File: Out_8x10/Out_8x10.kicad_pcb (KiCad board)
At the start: 2 copper layers, 100 x 100 mm, 162 parts, among them J1 Conn_01x06, J2 nmount SW Debug, J3 USB_C_Receptacle_USB2.0, J4 Conn_01x06, J5 Conn_01x09, J6 Conn_01x10, J7 Conn_01x09, J8 Conn_01x12, Q1 2N7002, Q10 AO3401A, Q11 AO3401A, Q12 AO3401A, Q13 2N7002, Q14 2N7002, Q15 AO3401A, Q16 AO3401A, Q17 AO3400A, Q18 AO3400A, Q19 AO3400A, Q2 2N7002, Q20 AO3400A, Q21 AO3400A, Q22 AO3400A, Q23 AO3400A, Q24 AO3400A, Q25 AO3400A, Q26 AO3400A, Q3 2N7002, Q4 AO3401A, Q5 AO3401A, Q6 AO3401A, Q7 2N7002, Q8 2N7002, Q9 2N7002, SW1 Reset, SW2 Boot, SW3 ADDRESS, U1 ADM3483, U10 L78L24_SOT89, U11 L78L24_SOT89, U12 L78L24_SOT89, U13 L78L24_SOT89, U2 W25Q128JVSIQ, U3 RP2040, U4 SN74AHCT1G125, U5 AP2112K-3.3, U6 L78L24_SOT89, U7 L78L24_SOT89, U8 L78L24_SOT89, U9 L78L24_SOT89, Y1 12MHz,18pF

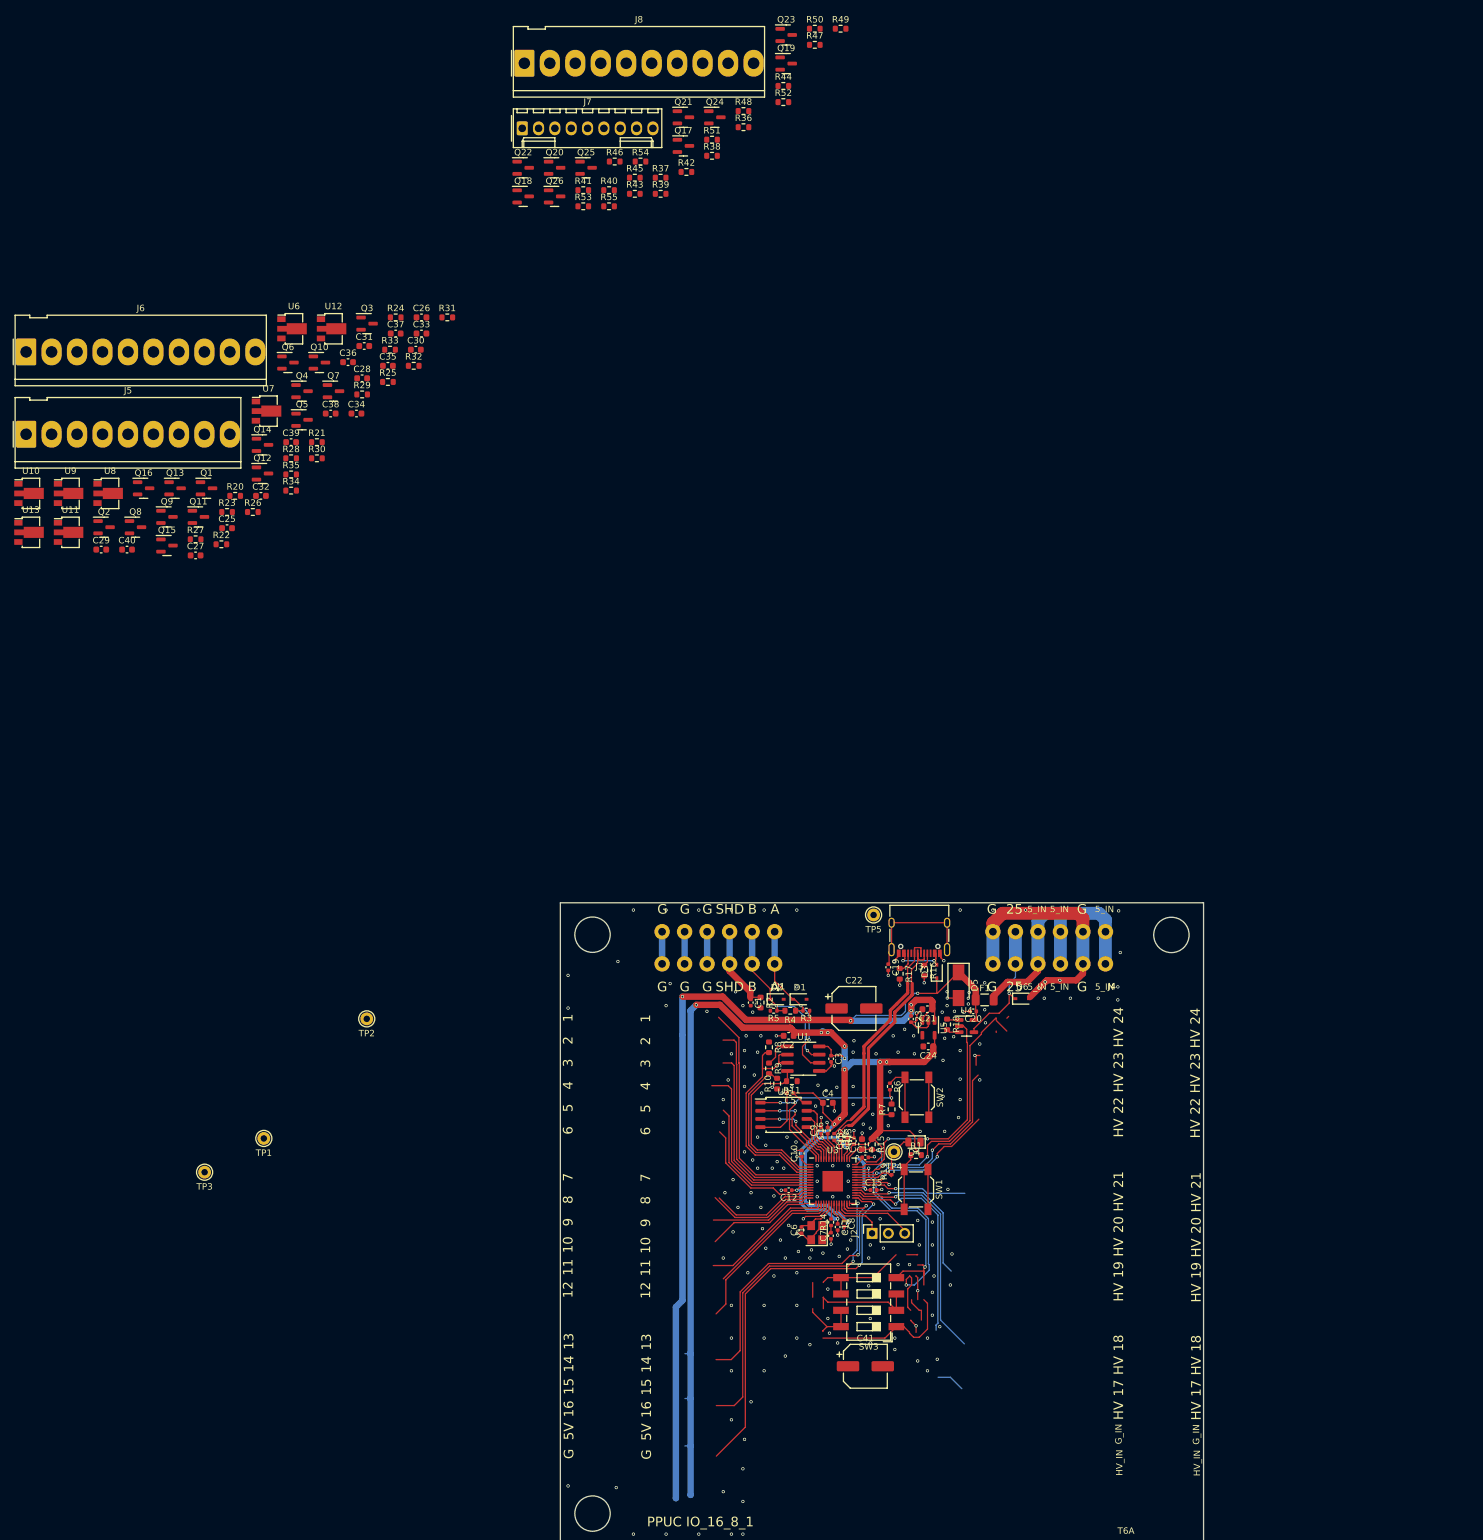
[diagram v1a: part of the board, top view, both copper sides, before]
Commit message: updated layout
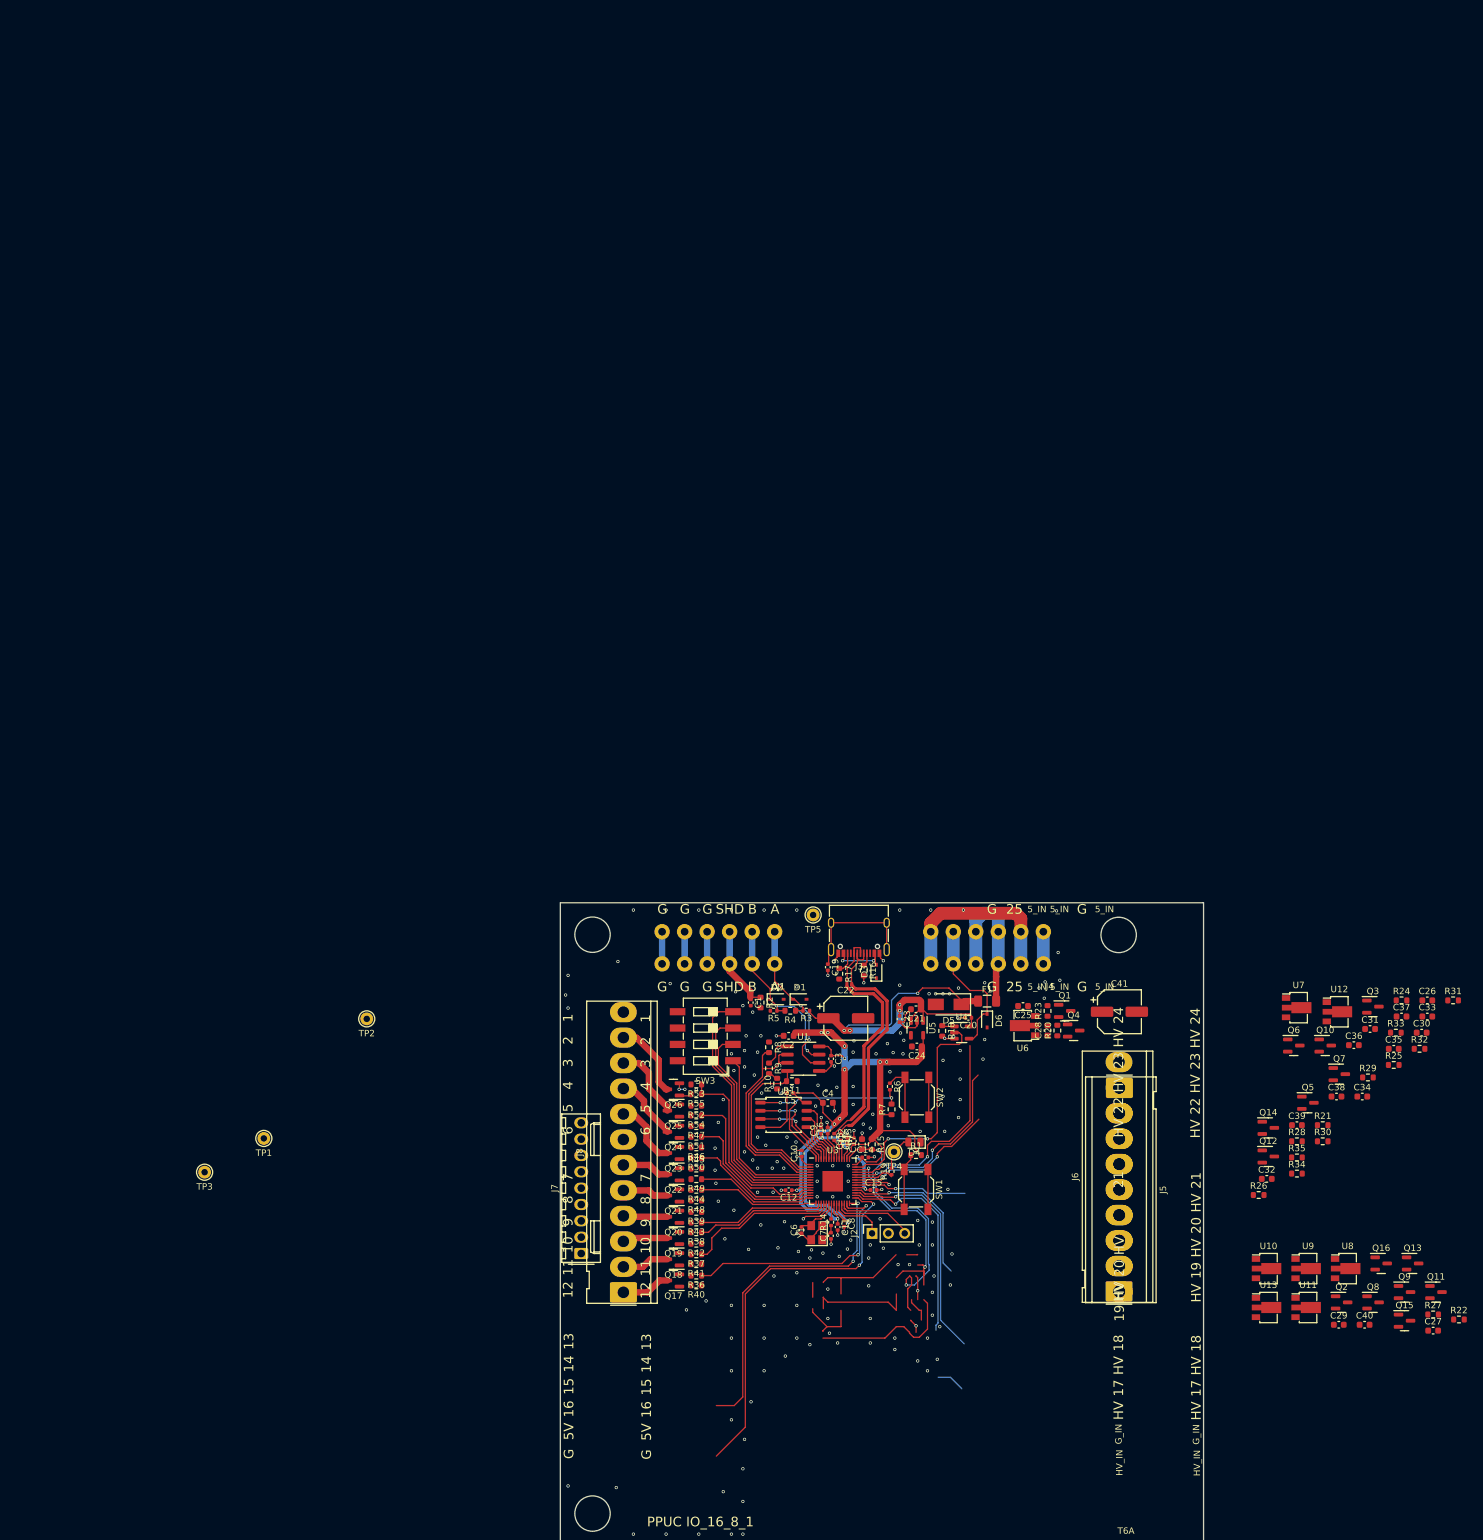
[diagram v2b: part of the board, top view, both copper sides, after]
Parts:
- J8: footprint Connector_Molex:Molex_KK-396_5273-10A_1x10_P3.96mm_Vertical -> Connector_Molex:Molex_KK-396_5273-12A_1x12_P3.96mm_Vertical
- moved C27 227.0 mm to (238.9, 111.3)
- moved R27 227.0 mm to (238.9, 108.8)
- moved U11 227.0 mm to (219.1, 107.7)
- moved U9 227.0 mm to (219.1, 101.7)
- moved C29 227.0 mm to (224.2, 110.4)
- moved C40 227.0 mm to (228.2, 110.4)
- moved Q11 227.0 mm to (239.3, 105.3)
- moved Q13 227.0 mm to (235.7, 100.9)
- moved Q15 227.0 mm to (234.4, 109.8)
- moved Q16 227.0 mm to (230.8, 100.9)
- moved Q2 227.0 mm to (224.7, 106.9)
- moved Q8 227.0 mm to (229.6, 106.9)
- moved Q9 227.0 mm to (234.4, 105.3)
- moved R22 227.0 mm to (242.9, 109.6)
- moved U10 227.0 mm to (213.0, 101.7)
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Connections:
- U3 pad 11: /Hi_6 -> /Lo_9
- U3 pad 12: /Hi_7 -> /Lo_8
- U3 pad 13: /Hi_8 -> /Lo_7
- U3 pad 14: /Lo_1 -> /Lo_6
- U3 pad 15: /Lo_2 -> /Lo_5
- U3 pad 16: /Lo_3 -> /Lo_4
- U3 pad 17: /Lo_4 -> /Lo_3
- U3 pad 18: /Lo_5 -> /Lo_2
- U3 pad 27: /Lo_6 -> /Lo_1
- U3 pad 28: /Lo_7 -> /Hi_1
- U3 pad 29: /Lo_8 -> /Hi_2
- U3 pad 30: /Lo_9 -> /Hi_3
- U3 pad 31: /Lo_10 -> /Hi_4
- U3 pad 32: /DIP_1 -> /Hi_5
- U3 pad 34: /DIP_2 -> /Hi_6
- U3 pad 35: /DIP_3 -> /Hi_7
- U3 pad 36: /DIP_4 -> /Hi_8
- U3 pad 5: /Hi_1 -> /DIP_1
- U3 pad 6: /Hi_2 -> /DIP_2
- U3 pad 7: /Hi_3 -> /DIP_3
- U3 pad 8: /Hi_4 -> /DIP_4
- U3 pad 9: /Hi_5 -> /Lo_10
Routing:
- net +3V3: track 244.5 -> 146.3 mm, vias 15 -> 14
- net +5V: track 161.7 -> 66.9 mm, vias 5 -> 7
- net /Lo_8: track 60.4 -> 23.2 mm, vias 2 -> 0
- net /DIP_2: track 17.7 -> 50.2 mm, vias 1 -> 0
- net GND: track 161.2 -> 130.6 mm, vias 206 -> 196
- net /Lo_7: track 50.7 -> 20.2 mm, vias 2 -> 0
- net /Lo_6: track 46.1 -> 18.7 mm, vias 2 -> 0
- net /Hi_2: track 33.1 -> 60.4 mm, vias 0 -> 2
- net /Lo_1: track 16.5 -> 37.6 mm, vias 0 -> 2
- net /20V: track 0.00 -> 20.7 mm
- net /5V_IN: track 43.1 -> 23.8 mm
- net /DIP_4: track 23.7 -> 40.8 mm, vias 2 -> 0
- net /Hi_1: track 35.4 -> 50.7 mm, vias 0 -> 2
- net /DIP_3: track 22.0 -> 37.2 mm, vias 1 -> 0
- net /Lo10/L10: track 0.00 -> 12.2 mm
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
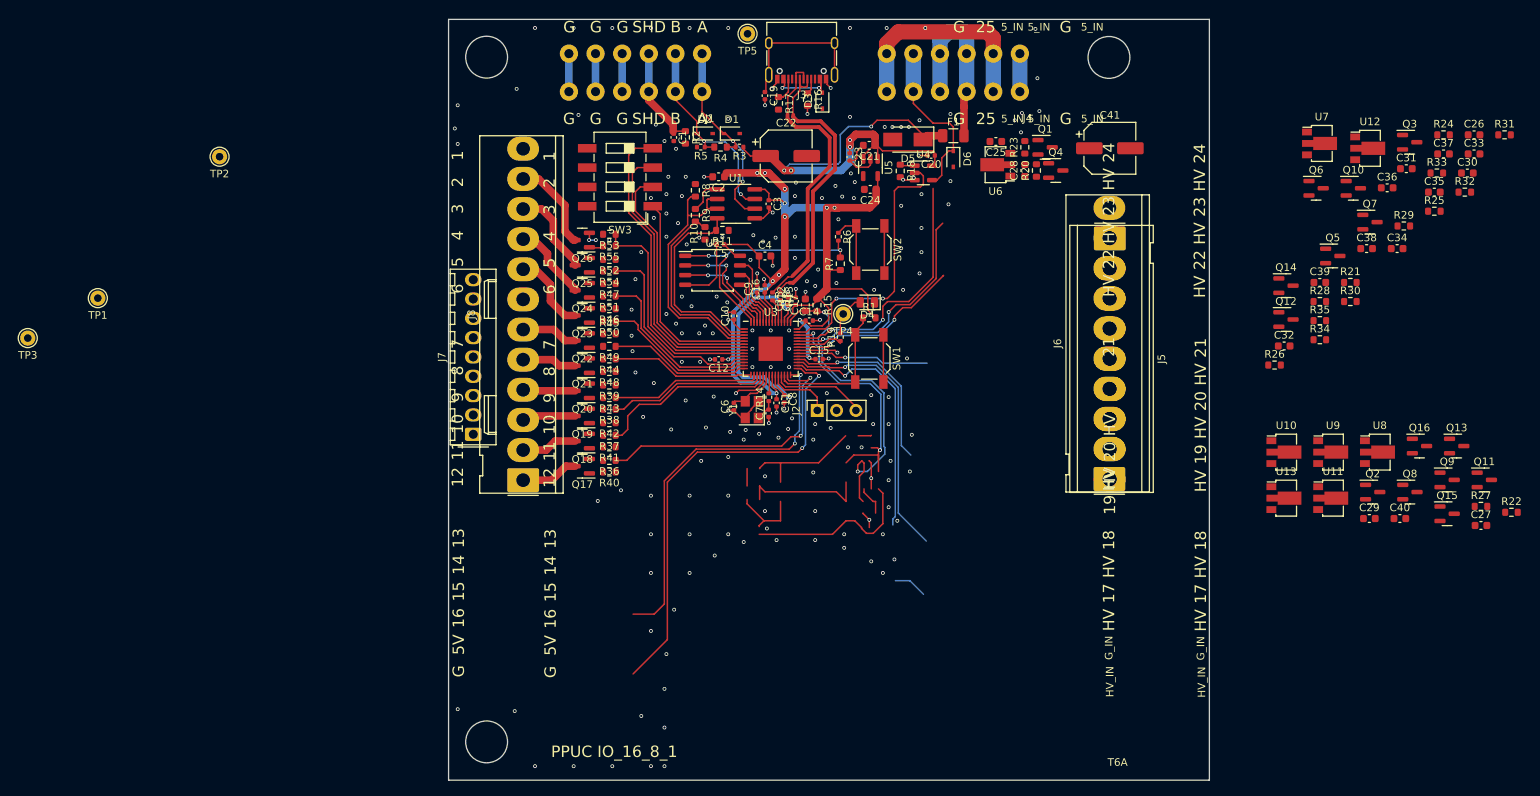
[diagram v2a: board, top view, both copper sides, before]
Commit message: updated layout
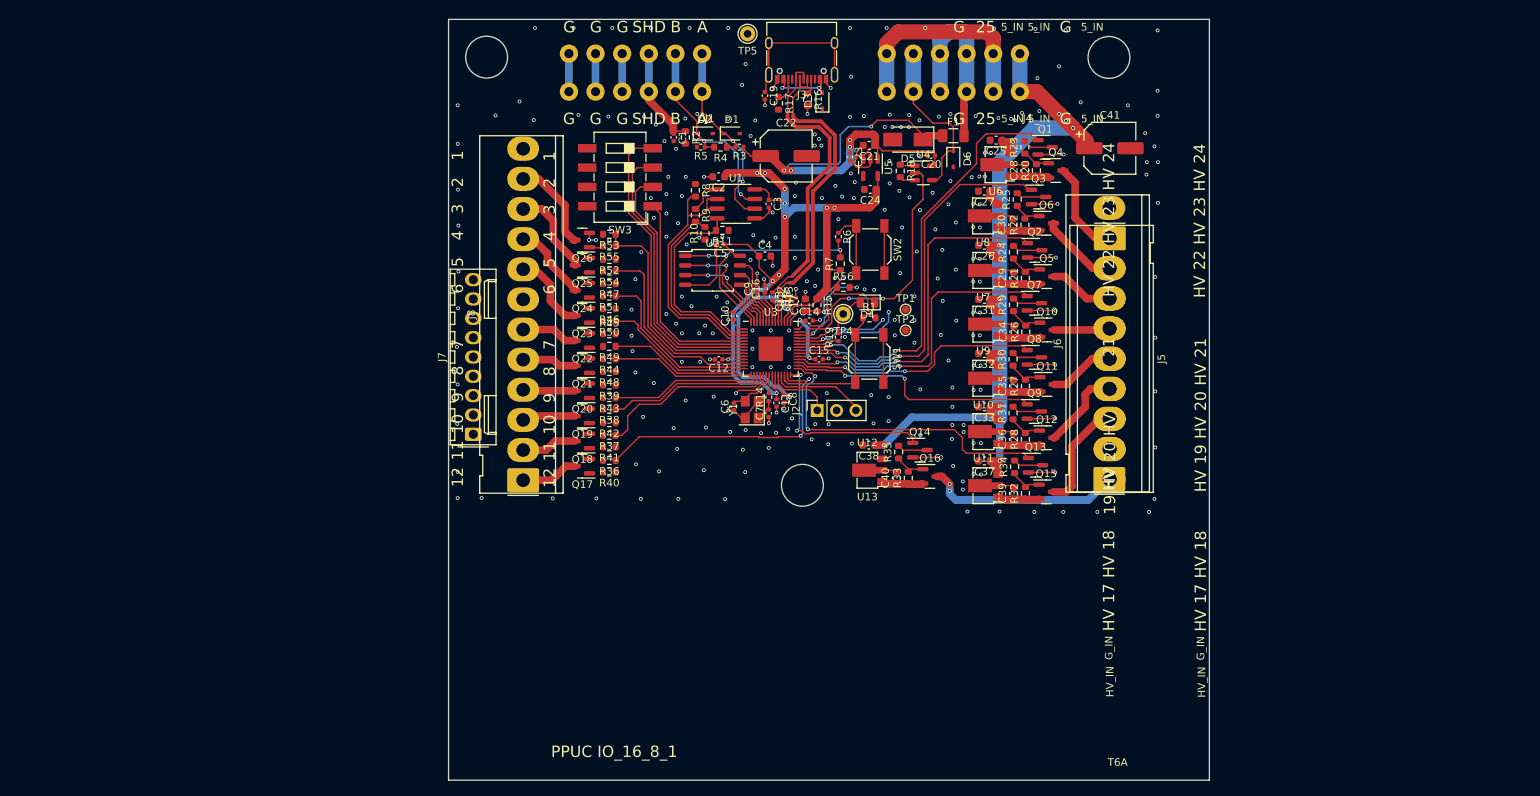
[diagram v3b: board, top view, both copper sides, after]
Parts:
- removed TP3: TP_IO28, Connector_Pin:Pin_D1.0mm_L10.0mm
- added R56: 10k, Resistor_SMD:R_0603_1608Metric, F.Cu at (155.1, 80.0)
- TP1, TP2: footprint Connector_Pin:Pin_D1.0mm_L10.0mm -> TestPoint:TestPoint_Pad_D1.0mm
- moved TP1 106.2 mm to (163.3, 82.9)
- moved TP2 93.0 mm to (163.3, 85.6)
- moved R33 80.2 mm to (163.6, 105.1), turned to 90 degrees
- moved C27 78.7 mm to (173.6, 67.4), turned to 180 degrees
- moved R22 74.3 mm to (179.0, 71.8), turned to 90 degrees
- moved R31 74.2 mm to (177.4, 96.5), turned to 90 degrees
- moved C37 72.6 mm to (173.6, 102.8), turned to 180 degrees
- moved C33 72.4 mm to (173.6, 95.7), turned to 180 degrees
- moved C38 70.3 mm to (158.4, 100.7), turned to 180 degrees
- moved R32 70.0 mm to (179.0, 107.1), turned to 90 degrees
- moved U12 67.0 mm to (173.8, 106.1), turned to 180 degrees
- moved C40 66.4 mm to (162.1, 105.1), turned to 90 degrees
- moved C26 66.0 mm to (173.6, 74.5), turned to 180 degrees
- moved Q16 64.5 mm to (166.5, 104.9)
- moved R27 61.9 mm to (179.0, 93.0), turned to 90 degrees
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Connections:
- U3 pad 28: /Hi_1 -> /Hi_8
- U3 pad 29: /Hi_2 -> /Hi_7
- U3 pad 30: /Hi_3 -> /Hi_6
- U3 pad 31: /Hi_4 -> /Hi_5
- U3 pad 32: /Hi_5 -> /Hi_4
- U3 pad 34: /Hi_6 -> /Hi_3
- U3 pad 35: /Hi_7 -> /Hi_2
- U3 pad 36: /Hi_8 -> /Hi_1
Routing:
- net /20V: track 20.7 -> 111.7 mm, vias 0 -> 11
- net /Hi_7: track 5.45 -> 41.9 mm, vias 1 -> 3
- net /3V3A: track 42.8 -> 12.3 mm
- net GND: track 130.6 -> 156.9 mm, vias 196 -> 276
- net /Hi8/H8: track 0.00 -> 25.8 mm, vias 0 -> 2
- net /DIP_1: track 50.9 -> 27.8 mm
- net Net-(TP2-Pad1): track 33.9 -> 12.3 mm
- net Net-(R56-Pad2): track 33.1 -> 13.2 mm
- net /DIP_2: track 50.2 -> 33.6 mm
- net /Hi_6: track 17.7 -> 33.7 mm, vias 1 -> 2
- net Net-(TP1-Pad1): track 30.1 -> 14.4 mm
- net /Hi8/H7: track 0.00 -> 14.4 mm
- net /Hi_3: track 33.0 -> 46.8 mm, vias 1 -> 2
- net /Hi8/H1: track 0.00 -> 12.5 mm
- net /Hi8/H6: track 0.00 -> 11.0 mm
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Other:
- board text removed: "13"
- board text removed: "14"
- board text removed: "15"
- board text removed: "16"
- board text removed: "5V"
